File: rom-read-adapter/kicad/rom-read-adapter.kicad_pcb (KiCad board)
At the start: 2 copper layers, 100 x 100 mm, 27 parts

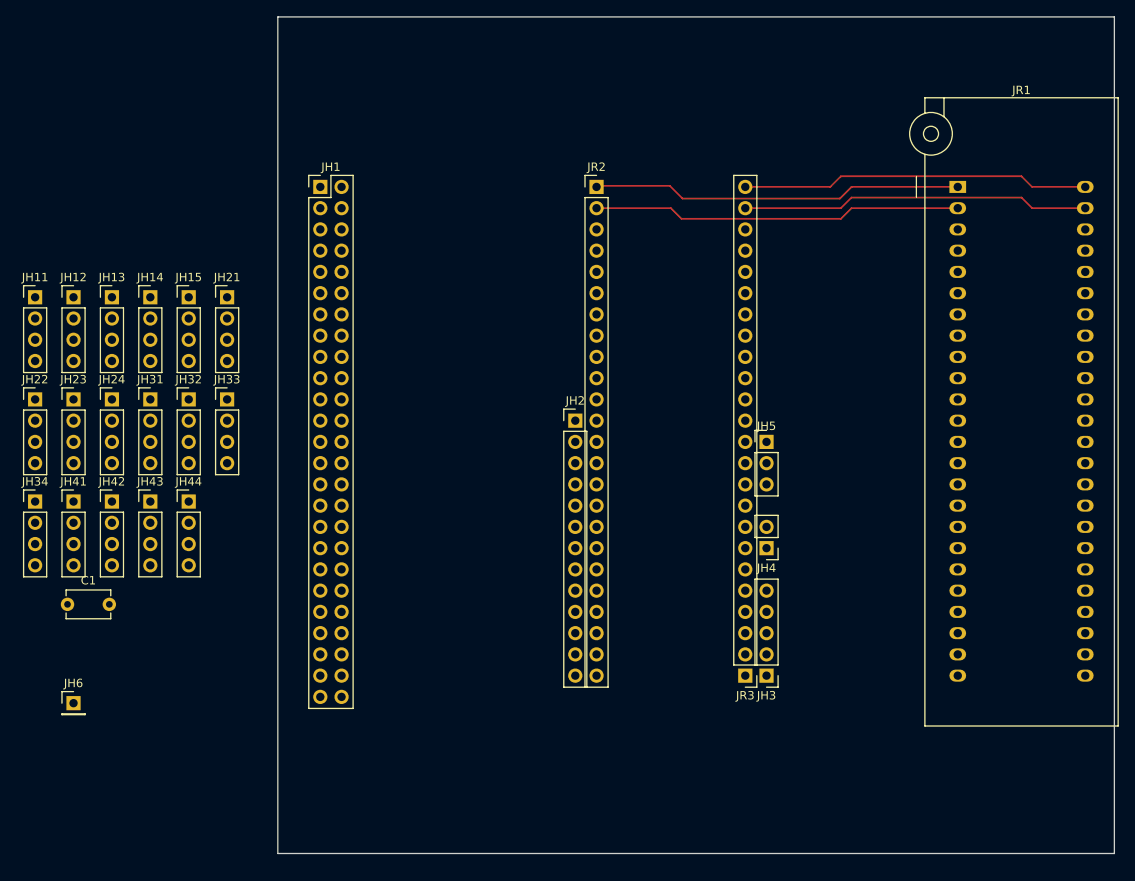
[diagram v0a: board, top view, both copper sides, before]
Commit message: WIP rom-read-adapter pcb: New layout and address pin silkscreens
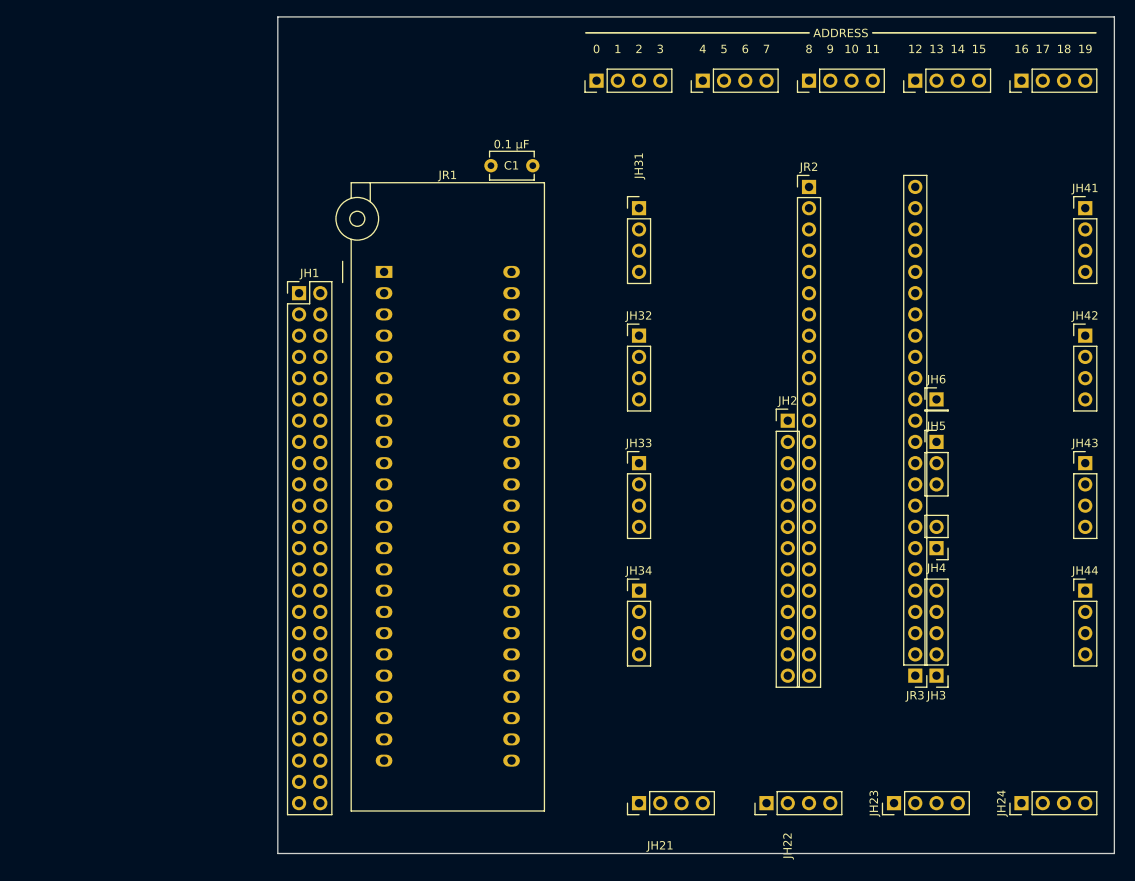
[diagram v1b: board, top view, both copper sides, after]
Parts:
- moved JH41 125.9 mm to (198.1, 73.7)
- moved JH24 119.0 mm to (190.5, 144.8), turned to 90 degrees
- moved JH42 118.0 mm to (198.1, 88.9)
- moved JH43 111.9 mm to (198.1, 104.1)
- moved JH6 109.4 mm to (180.3, 96.5)
- moved JH23 109.3 mm to (175.3, 144.8), turned to 90 degrees
- moved JH44 107.7 mm to (198.1, 119.4)
- moved JH15 102.9 mm to (190.5, 58.4), turned to 90 degrees
- moved JH22 99.9 mm to (160.0, 144.8), turned to 90 degrees
- moved JH14 95.0 mm to (177.8, 58.4), turned to 90 degrees
- moved JH13 87.3 mm to (165.1, 58.4), turned to 90 degrees
- moved JH12 79.6 mm to (152.4, 58.4), turned to 90 degrees
- moved JH21 78.0 mm to (144.8, 144.8), turned to 90 degrees
- moved JH34 73.0 mm to (144.8, 119.4)
- moved C1 72.9 mm to (127.1, 68.6)
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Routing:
- net Net-(JR1-Pin_1): track 44.4 -> 0.00 mm
- net Net-(JR1-Pin_2): track 44.2 -> 0.00 mm
- net Net-(JR1-Pin_48): track 41.7 -> 0.00 mm
- net Net-(JR1-Pin_47): track 41.7 -> 0.00 mm
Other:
- board text added: "0"
- board text added: "1"
- board text added: "10"
- board text added: "11"
- board text added: "12"
- board text added: "13"
- board text added: "14"
- board text added: "15"
- board text added: "16"
- board text added: "17"
- board text added: "18"
- board text added: "19"
- board text added: "2"
- board text added: "3"
- board text added: "4"
- board text added: "5"
- board text added: "6"
- board text added: "7"
- board text added: "8"
- board text added: "9"
- board text added: "ADDRESS"

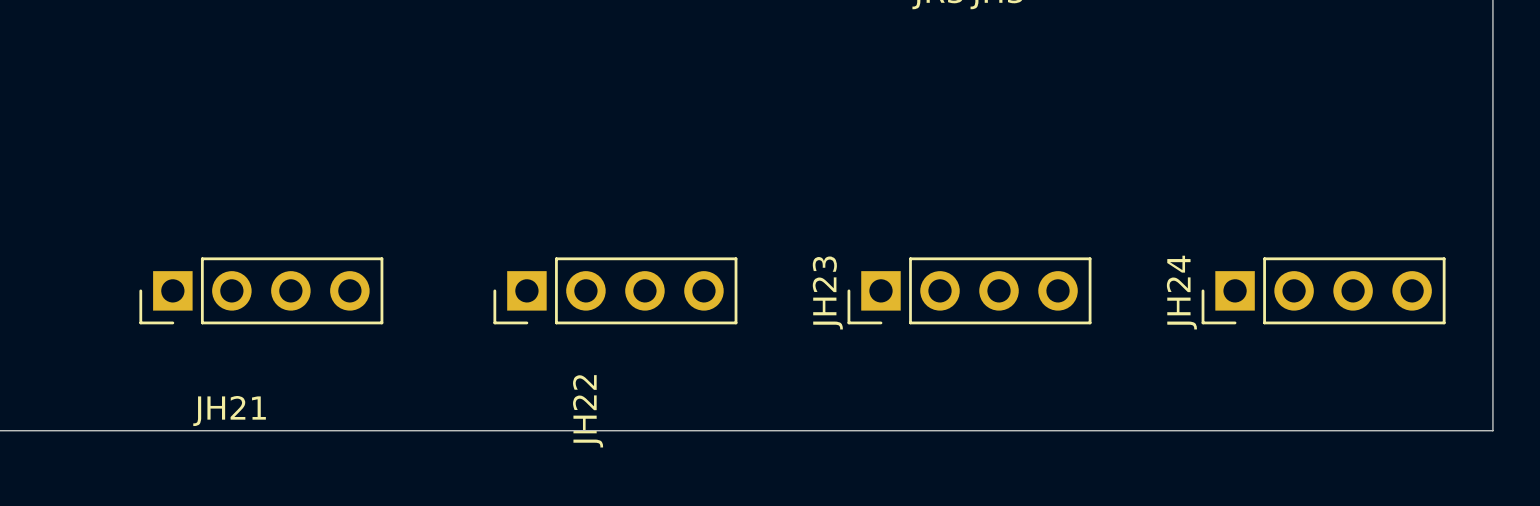
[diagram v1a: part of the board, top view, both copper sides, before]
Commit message: WIP rom-read-adapter pcb: Add lkscreen for data pins
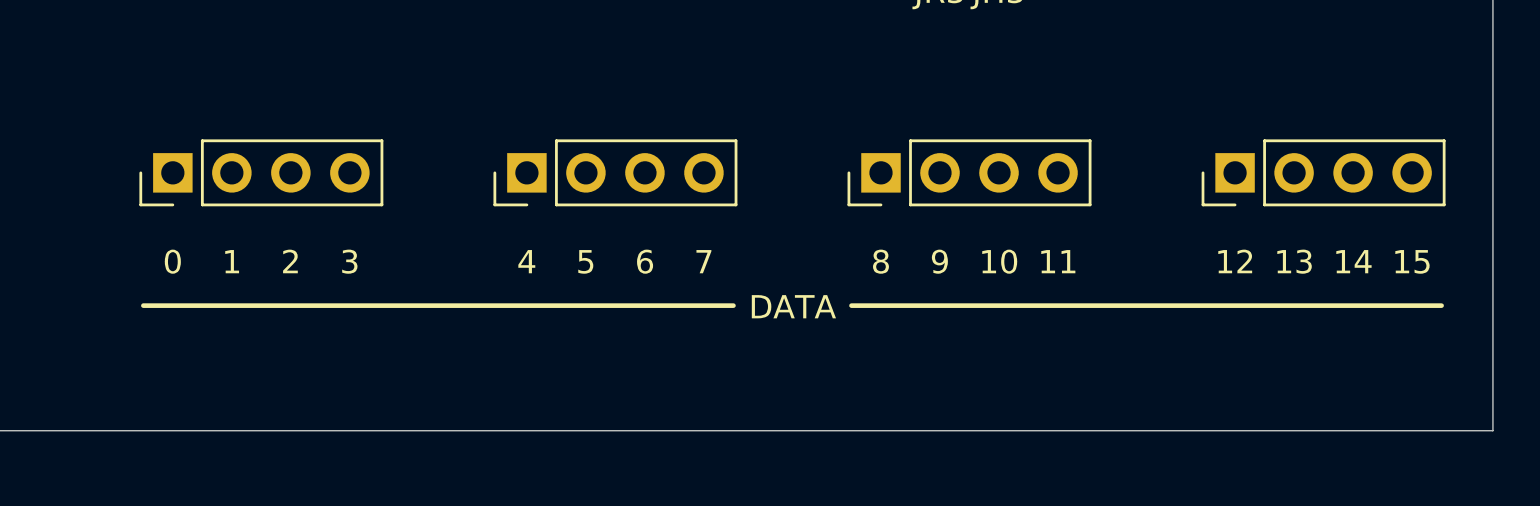
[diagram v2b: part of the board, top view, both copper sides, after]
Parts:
- moved JH21 5.08 mm to (144.8, 139.7)
- moved JH22 5.08 mm to (160.0, 139.7)
- moved JH23 5.08 mm to (175.3, 139.7)
- moved JH24 5.08 mm to (190.5, 139.7)
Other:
- board text added: "DATA"
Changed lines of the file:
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@@
 	(footprint "Connector_PinHeader_2.54mm:PinHeader_1x04_P2.54mm_Vertical"
 		(layer "F.Cu")
-		(at 175.26 144.78 90)
+		(at 175.26 139.7 90)
 		(descr "Through hole straight pin header, 1x04, 2.54mm pitch, single row")
 		(tags "Through hole pin header THT 1x04 2.54mm single row")
@@
 			(at 0 -2.38 90)
 			(layer "F.SilkS")
+			(hide yes)
 			(effects
 				(font
@@
 	(footprint "Connector_PinHeader_2.54mm:PinHeader_1x04_P2.54mm_Vertical"
 		(layer "F.Cu")
-		(at 160.02 144.78 90)
+		(at 160.02 139.7 90)
 		(descr "Through hole straight pin header, 1x04, 2.54mm pitch, single row")
 		(tags "Through hole pin header THT 1x04 2.54mm single row")
@@
 			(at -5.08 2.54 90)
 			(layer "F.SilkS")
+			(hide yes)
 			(effects
 				(font
@@
 	(footprint "Connector_PinHeader_2.54mm:PinHeader_1x04_P2.54mm_Vertical"
 		(layer "F.Cu")
-		(at 190.5 144.78 90)
+		(at 190.5 139.7 90)
 		(descr "Through hole straight pin header, 1x04, 2.54mm pitch, single row")
 		(tags "Through hole pin header THT 1x04 2.54mm single row")
@@
 			(at 0 -2.38 90)
 			(layer "F.SilkS")
+			(hide yes)
 			(effects
 				(font
@@
 	(footprint "Connector_PinHeader_2.54mm:PinHeader_1x04_P2.54mm_Vertical"
 		(layer "F.Cu")
-		(at 144.78 144.78 90)
+		(at 144.78 139.7 90)
 		(descr "Through hole straight pin header, 1x04, 2.54mm pitch, single row")
 		(tags "Through hole pin header THT 1x04 2.54mm single row")
@@
 			(at -5.08 2.54 180)
 			(layer "F.SilkS")
+			(hide yes)
 			(effects
 				(font
@@
 	)
 	(gr_line
+		(start 143.51 145.415)
+		(end 168.91 145.415)
+		(stroke
+			(width 0.2)
+			(type solid)
+		)
+		(layer "F.SilkS")
+	)
+	(gr_line
+		(start 173.99 145.415)
+		(end 199.39 145.415)
+		(stroke
+			(width 0.2)
+			(type solid)
+		)
+		(layer "F.SilkS")
+	)
+	(gr_line
 		(start 172.72 52.705)
 		(end 199.39 52.705)
@@
 		(layer "Edge.Cuts")
 	)
+	(gr_text "2"
+		(at 149.86 144.145 0)
+		(layer "F.SilkS")
+		(effects
+			(font
+				(size 1 1)
+				(thickness 0.15)
+			)
+			(justify bottom)
+		)
+	)
+	(gr_text "8"
+		(at 175.26 144.145 0)
+		(layer "F.SilkS")
+		(effects
+			(font
+				(size 1 1)
+				(thickness 0.15)
+			)
+			(justify bottom)
+		)
+	)
+	(gr_text "14"
+		(at 195.58 144.145 0)
+		(layer "F.SilkS")
+		(effects
+			(font
+				(size 1 1)
+				(thickness 0.15)
+			)
+			(justify bottom)
+		)
+	)
 	(gr_text "14"
 		(at 182.88 55.245 0)
@@
 		)
 	)
+	(gr_text "4"
+		(at 160.02 144.145 0)
+		(layer "F.SilkS")
+		(effects
+			(font
+				(size 1 1)
+				(thickness 0.15)
+			)
+			(justify bottom)
+		)
+	)
+	(gr_text "11"
+		(at 182.88 144.145 0)
+		(layer "F.SilkS")
+		(effects
+			(font
+				(size 1 1)
+				(thickness 0.15)
+			)
+			(justify bottom)
+		)
+	)
 	(gr_text "5"
 		(at 154.94 55.245 0)
@@
 		)
 	)
+	(gr_text "13"
+		(at 193.04 144.145 0)
+		(layer "F.SilkS")
+		(effects
+			(font
+				(size 1 1)
+				(thickness 0.15)
+			)
+			(justify bottom)
+		)
+	)
 	(gr_text "1"
 		(at 142.24 55.245 0)
@@
 		)
 	)
+	(gr_text "0"
+		(at 144.78 144.145 0)
+		(layer "F.SilkS")
+		(effects
+			(font
+				(size 1 1)
+				(thickness 0.15)
+			)
+			(justify bottom)
+		)
+	)
+	(gr_text "DATA"
+		(at 171.45 146.084592 0)
+		(layer "F.SilkS")
+		(effects
+			(font
+				(size 1 1)
+				(thickness 0.15)
+			)
+			(justify bottom)
+		)
+	)
 	(gr_text "16"
 		(at 190.5 55.245 0)
@@
 		)
 	)
+	(gr_text "7"
+		(at 167.64 144.145 0)
+		(layer "F.SilkS")
+		(effects
+			(font
+				(size 1 1)
+				(thickness 0.15)
+			)
+			(justify bottom)
+		)
+	)
 	(gr_text "17"
 		(at 193.04 55.245 0)
@@
 		)
 	)
+	(gr_text "1"
+		(at 147.32 144.145 0)
+		(layer "F.SilkS")
+		(effects
+			(font
+				(size 1 1)
+				(thickness 0.15)
+			)
+			(justify bottom)
+		)
+	)
+	(gr_text "9"
+		(at 177.8 144.145 0)
+		(layer "F.SilkS")
+		(effects
+			(font
+				(size 1 1)
+				(thickness 0.15)
+			)
+			(justify bottom)
+		)
+	)
 	(gr_text "19"
 		(at 198.12 55.245 0)
@@
 		)
 	)
+	(gr_text "12"
+		(at 190.5 144.145 0)
+		(layer "F.SilkS")
+		(effects
+			(font
+				(size 1 1)
+				(thickness 0.15)
+			)
+			(justify bottom)
+		)
+	)
 	(gr_text "7"
 		(at 160.02 55.245 0)
@@
 		)
 	)
+	(gr_text "10"
+		(at 180.34 144.145 0)
+		(layer "F.SilkS")
+		(effects
+			(font
+				(size 1 1)
+				(thickness 0.15)
+			)
+			(justify bottom)
+		)
+	)
+	(gr_text "6"
+		(at 165.1 144.145 0)
+		(layer "F.SilkS")
+		(effects
+			(font
+				(size 1 1)
+				(thickness 0.15)
+			)
+			(justify bottom)
+		)
+	)
 	(gr_text "12"
 		(at 177.8 55.245 0)
@@
 		)
 	)
+	(gr_text "5"
+		(at 162.56 144.145 0)
+		(layer "F.SilkS")
+		(effects
+			(font
+				(size 1 1)
+				(thickness 0.15)
+			)
+			(justify bottom)
+		)
+	)
 	(gr_text "2"
 		(at 144.78 55.245 0)
 		(layer "F.SilkS")
 		(effects
+			(font
+				(size 1 1)
+				(thickness 0.15)
+			)
+			(justify bottom)
+		)
+	)
+	(gr_text "3"
+		(at 152.4 144.145 0)
+		(layer "F.SilkS")
+		(effects
+			(font
+				(size 1 1)
+				(thickness 0.15)
+			)
+			(justify bottom)
+		)
+	)
+	(gr_text "15"
+		(at 198.12 144.145 0)
+		(layer "F.SilkS")
+		(effects

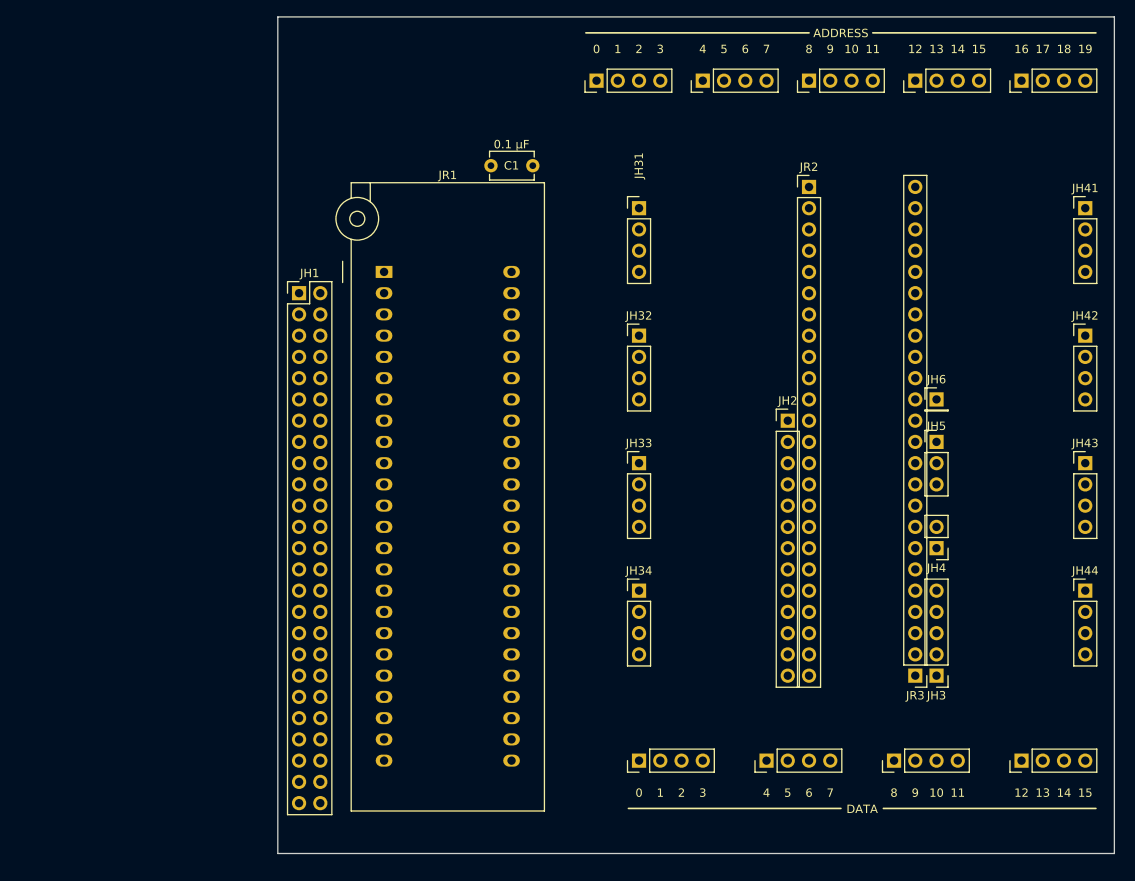
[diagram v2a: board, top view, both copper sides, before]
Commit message: WIP rom-read-adapter pcb: Finish host side labels
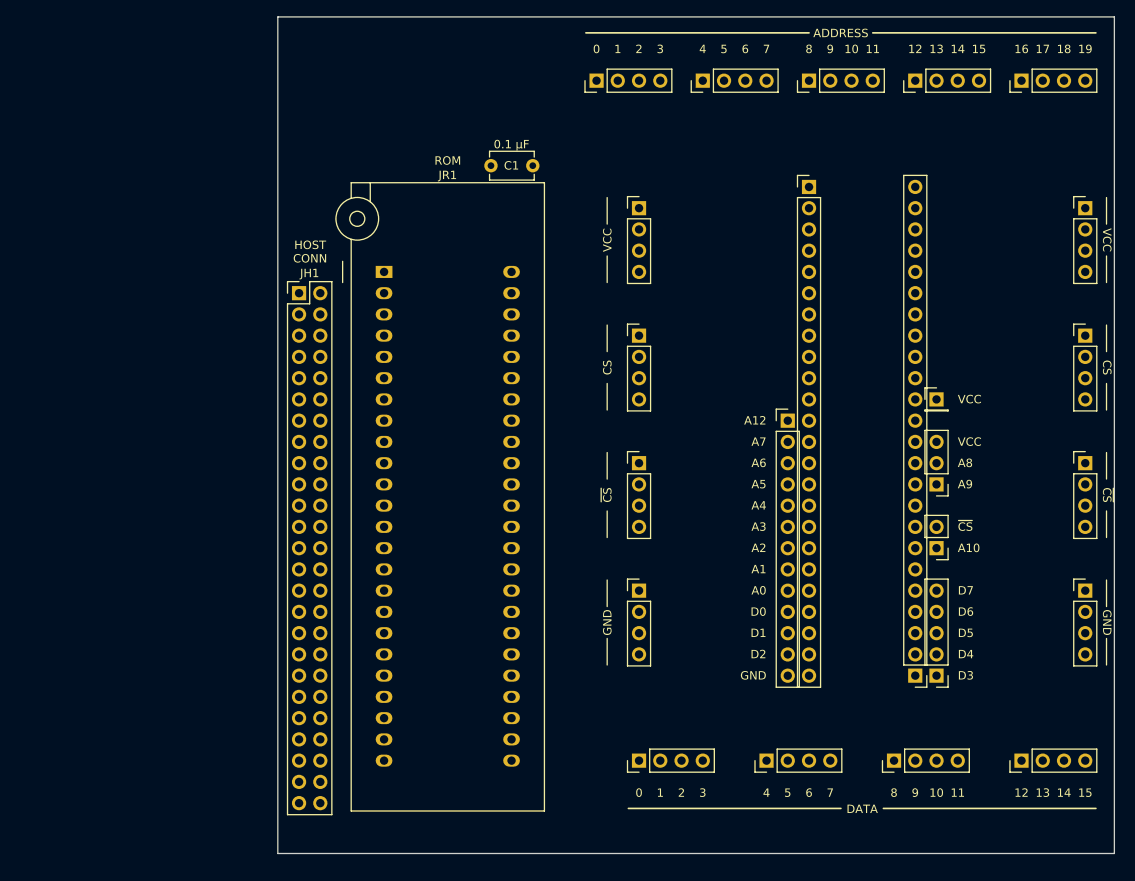
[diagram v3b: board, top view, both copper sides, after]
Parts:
- moved JH5 5.08 mm to (180.3, 106.7), turned to 180 degrees
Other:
- board text added: "A0"
- board text added: "A1"
- board text added: "A10"
- board text added: "A12"
- board text added: "A2"
- board text added: "A3"
- board text added: "A4"
- board text added: "A5"
- board text added: "A6"
- board text added: "A7"
- board text added: "A8"
- board text added: "A9"
- board text added: "CS"
- board text added: "D0"
- board text added: "D1"
- board text added: "D2"
- board text added: "D3"
- board text added: "D4"
- board text added: "D5"
- board text added: "D6"
- board text added: "D7"
- board text added: "GND"
- board text added: "HOST CONN"
- board text added: "ROM"
- board text added: "VCC"
- board text added: "~{CS}"
